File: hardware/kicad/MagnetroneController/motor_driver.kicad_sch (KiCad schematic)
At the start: 3 parts, among them J1 Conn_01x04

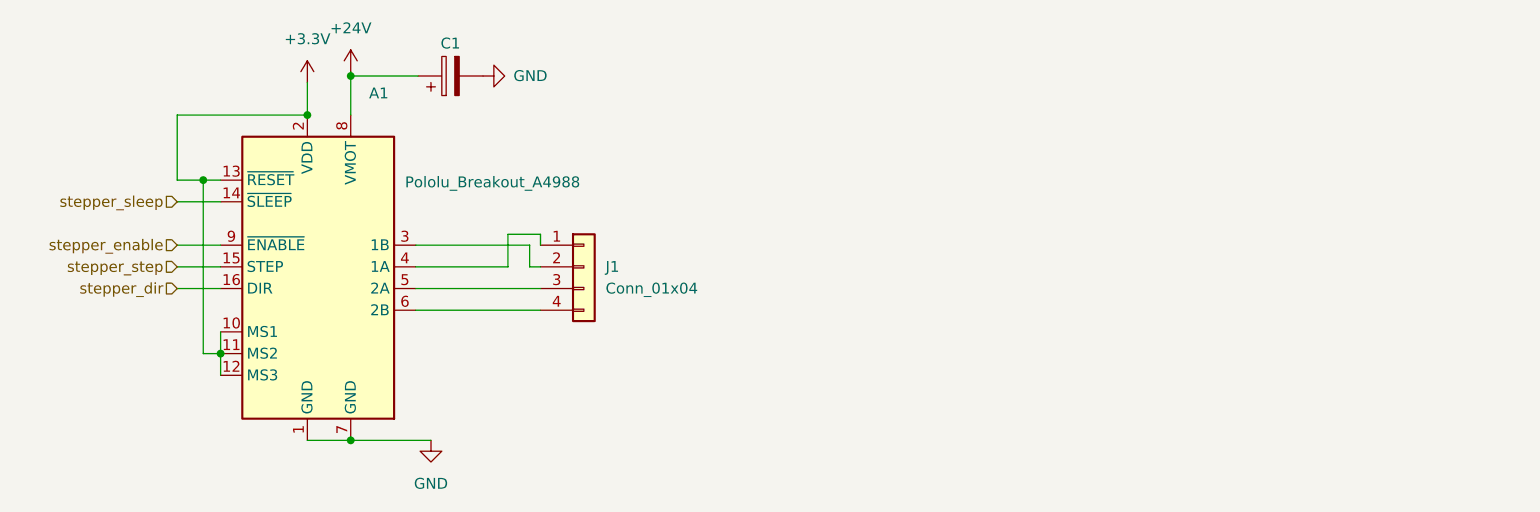
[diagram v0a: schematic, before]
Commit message: chore: replace motor driver
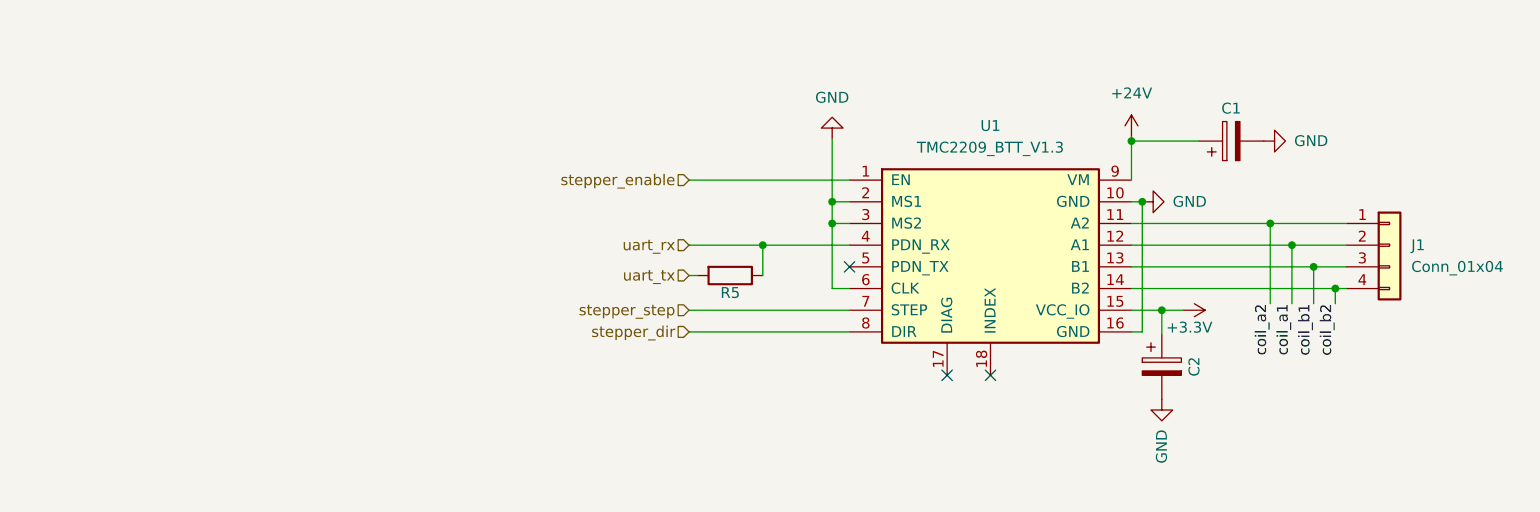
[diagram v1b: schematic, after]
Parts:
- removed A1: Pololu_Breakout_A4988, Module:Pololu_Breakout-16_15.2x20.3mm, symbol Driver_Motor:Pololu_Breakout_A4988
- added C2: 100uf, Capacitor_THT:CP_Radial_D8.0mm_P3.80mm, symbol Device:C_Polarized
- added R5: 1k, Resistor_SMD:R_0805_2012Metric_Pad1.20x1.40mm_HandSolder, symbol Device:R
- added U1: TMC2209_BTT_V1.3, magnetrone:TMC2209_BTT_V1.3, symbol magnetrone:TMC2209_BTT_V1.3
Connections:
- net +24V: now also U1.9 (VM)
- net +3.3V: now also C2.1, U1.15 (VCC_IO)
- net GND: now also C2.2, U1.10 (GND), U1.16 (GND), U1.2 (MS1), U1.3 (MS2), U1.6 (CLK)
- net stepper_dir: now also U1.8 (DIR)
- net stepper_enable: now also U1.1 (EN)
- net stepper_step: now also U1.7 (STEP)
- net coil_a1: now reaches J1.2 (Pin_2)
- net coil_a1: now also U1.12 (A1)
- net coil_a2: now reaches J1.1 (Pin_1)
- net coil_a2: now also U1.11 (A2)
- net coil_b1: now reaches J1.3 (Pin_3)
- net coil_b1: now also U1.13 (B1)
- net coil_b2: now reaches J1.4 (Pin_4)
- net coil_b2: now also U1.14 (B2)
- new net uart_rx: R5.1, U1.4 (PDN_RX)
- new net uart_tx: R5.2
- no-connect marks 0 -> 3
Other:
- moved on the sheet: C1, J1
